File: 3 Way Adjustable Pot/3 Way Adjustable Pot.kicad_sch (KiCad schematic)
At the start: 26 parts, among them SW1 SW_MEC_5E, SW2 SW_MEC_5E, SW3 SW_MEC_5E, SW4 SW_MEC_5E, U1 74HC14, U2 74LS28, U3 74HC74, U4 74HC14, U6 74LS157, U7 LM555xN

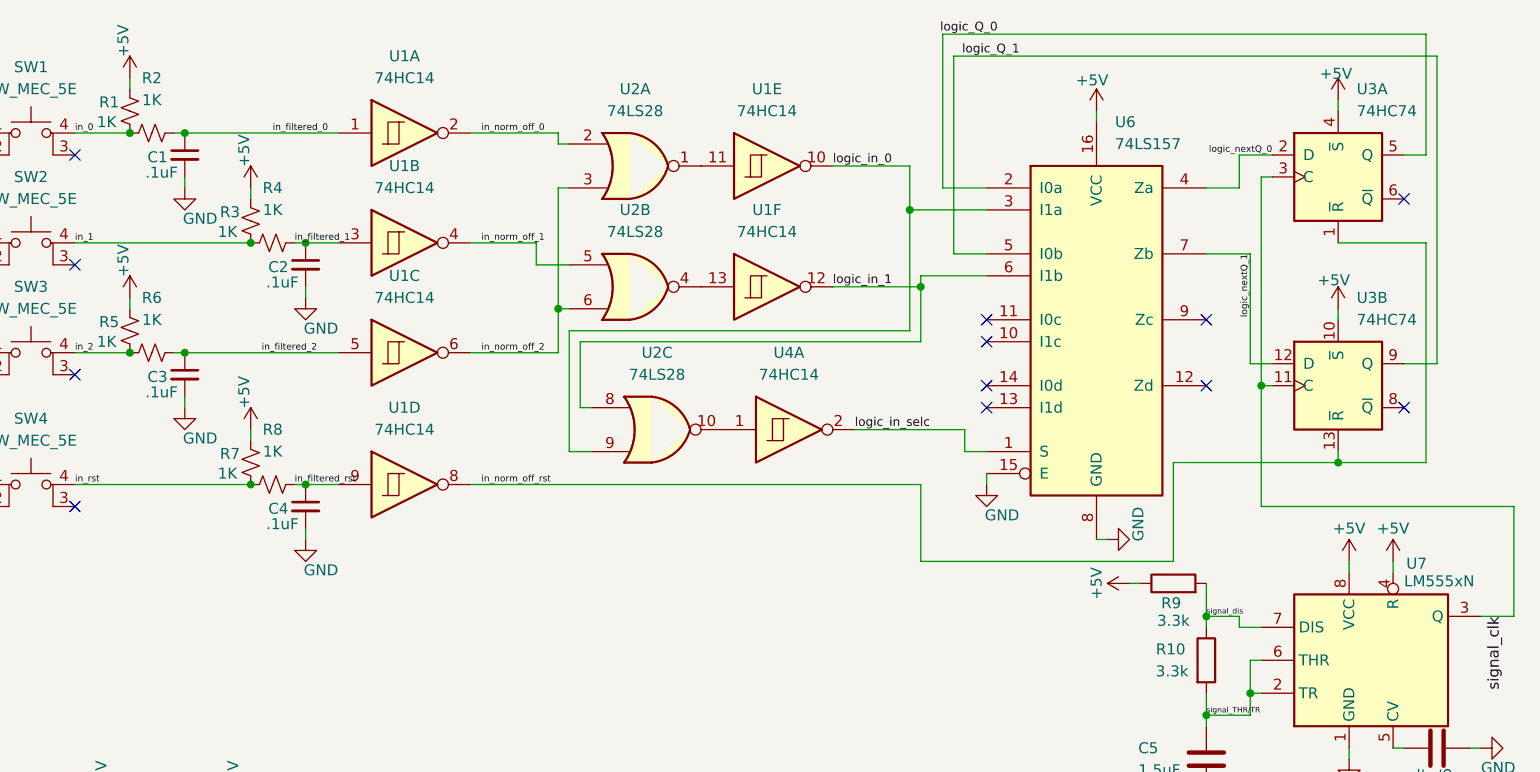
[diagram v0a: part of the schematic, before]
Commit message: add commits to 3 way adjustable pot
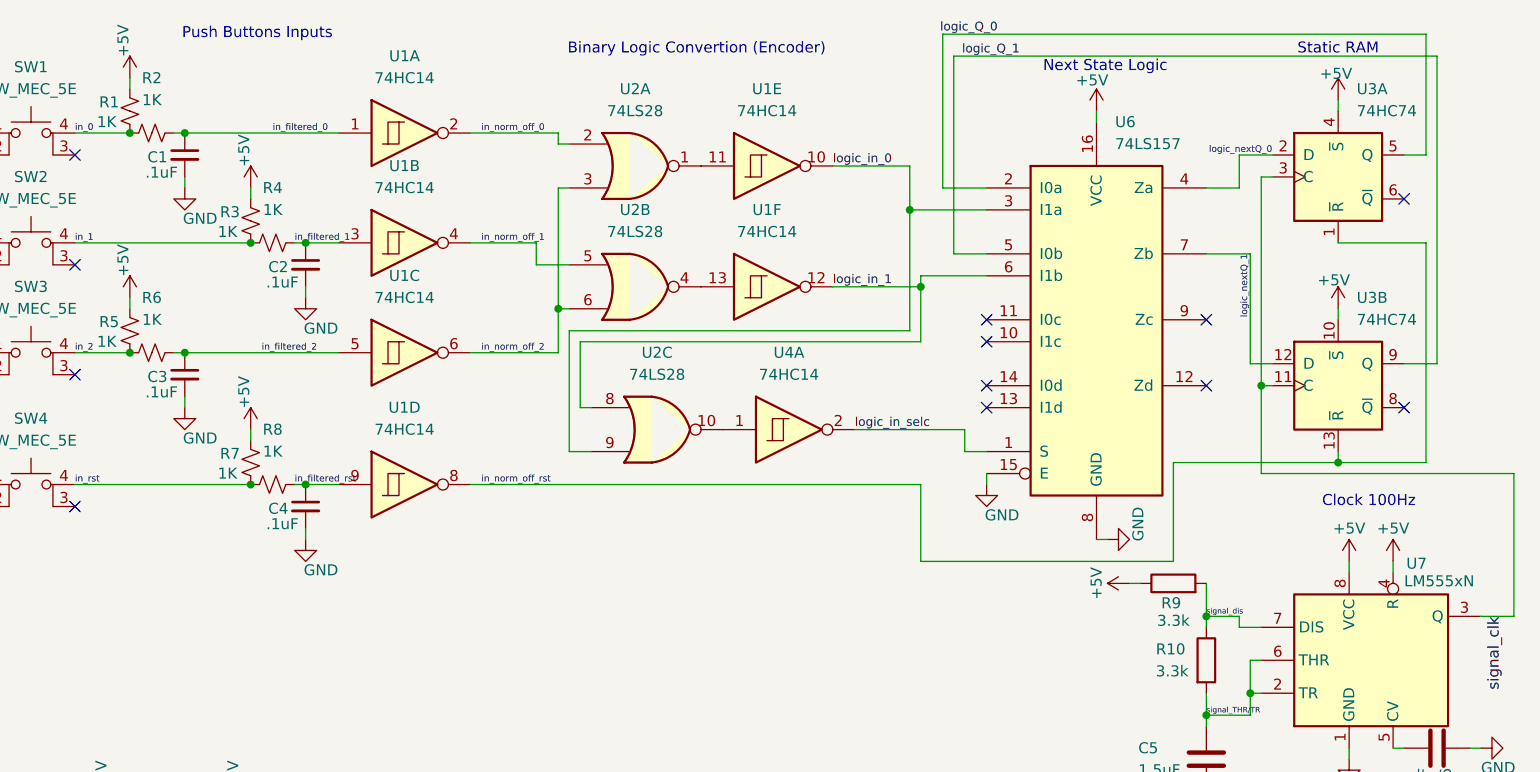
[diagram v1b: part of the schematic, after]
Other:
- note added: "Binary Logic Convertion (Encoder)"
- note added: "Clock 100Hz"
- note added: "Next State Logic"
- note added: "Push Buttons Inputs"
- note added: "Static RAM"
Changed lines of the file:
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@@
 		(rev "1")
 	)
+	(text "Push Buttons Inputs\n "
+		(exclude_from_sim no)
+		(at 51.562 14.986 0)
+		(effects
+			(font
+				(size 1.27 1.27)
+			)
+		)
+	)
+	(text "Clock 100Hz"
+		(exclude_from_sim no)
+		(at 180.086 68.072 0)
+		(effects
+			(font
+				(size 1.27 1.27)
+			)
+		)
+	)
+	(text "Binary Logic Convertion (Encoder)\n"
+		(exclude_from_sim no)
+		(at 102.362 15.748 0)
+		(effects
+			(font
+				(size 1.27 1.27)
+			)
+		)
+	)
+	(text "Static RAM"
+		(exclude_from_sim no)
+		(at 176.53 15.748 0)
+		(effects
+			(font
+				(size 1.27 1.27)
+			)
+		)
+	)
+	(text "Next State Logic \n"
+		(exclude_from_sim no)
+		(at 149.606 17.78 0)
+		(effects
+			(font
+				(size 1.27 1.27)
+			)
+		)
+	)
 	(junction
 		(at 36.83 25.4)
@@
 	(wire
 		(pts
-			(xy 196.85 81.28) (xy 196.85 68.58)
+			(xy 196.85 81.28) (xy 196.85 64.77)
 		)
 		(stroke
@@
 	(wire
 		(pts
-			(xy 167.64 54.61) (xy 167.64 68.58)
+			(xy 167.64 54.61) (xy 167.64 64.77)
 		)
 		(stroke
@@
 	(wire
 		(pts
-			(xy 196.85 68.58) (xy 167.64 68.58)
-		)
-		(stroke
+			(xy 196.85 64.77) (xy 167.64 64.77)
+		)
+		(stroke

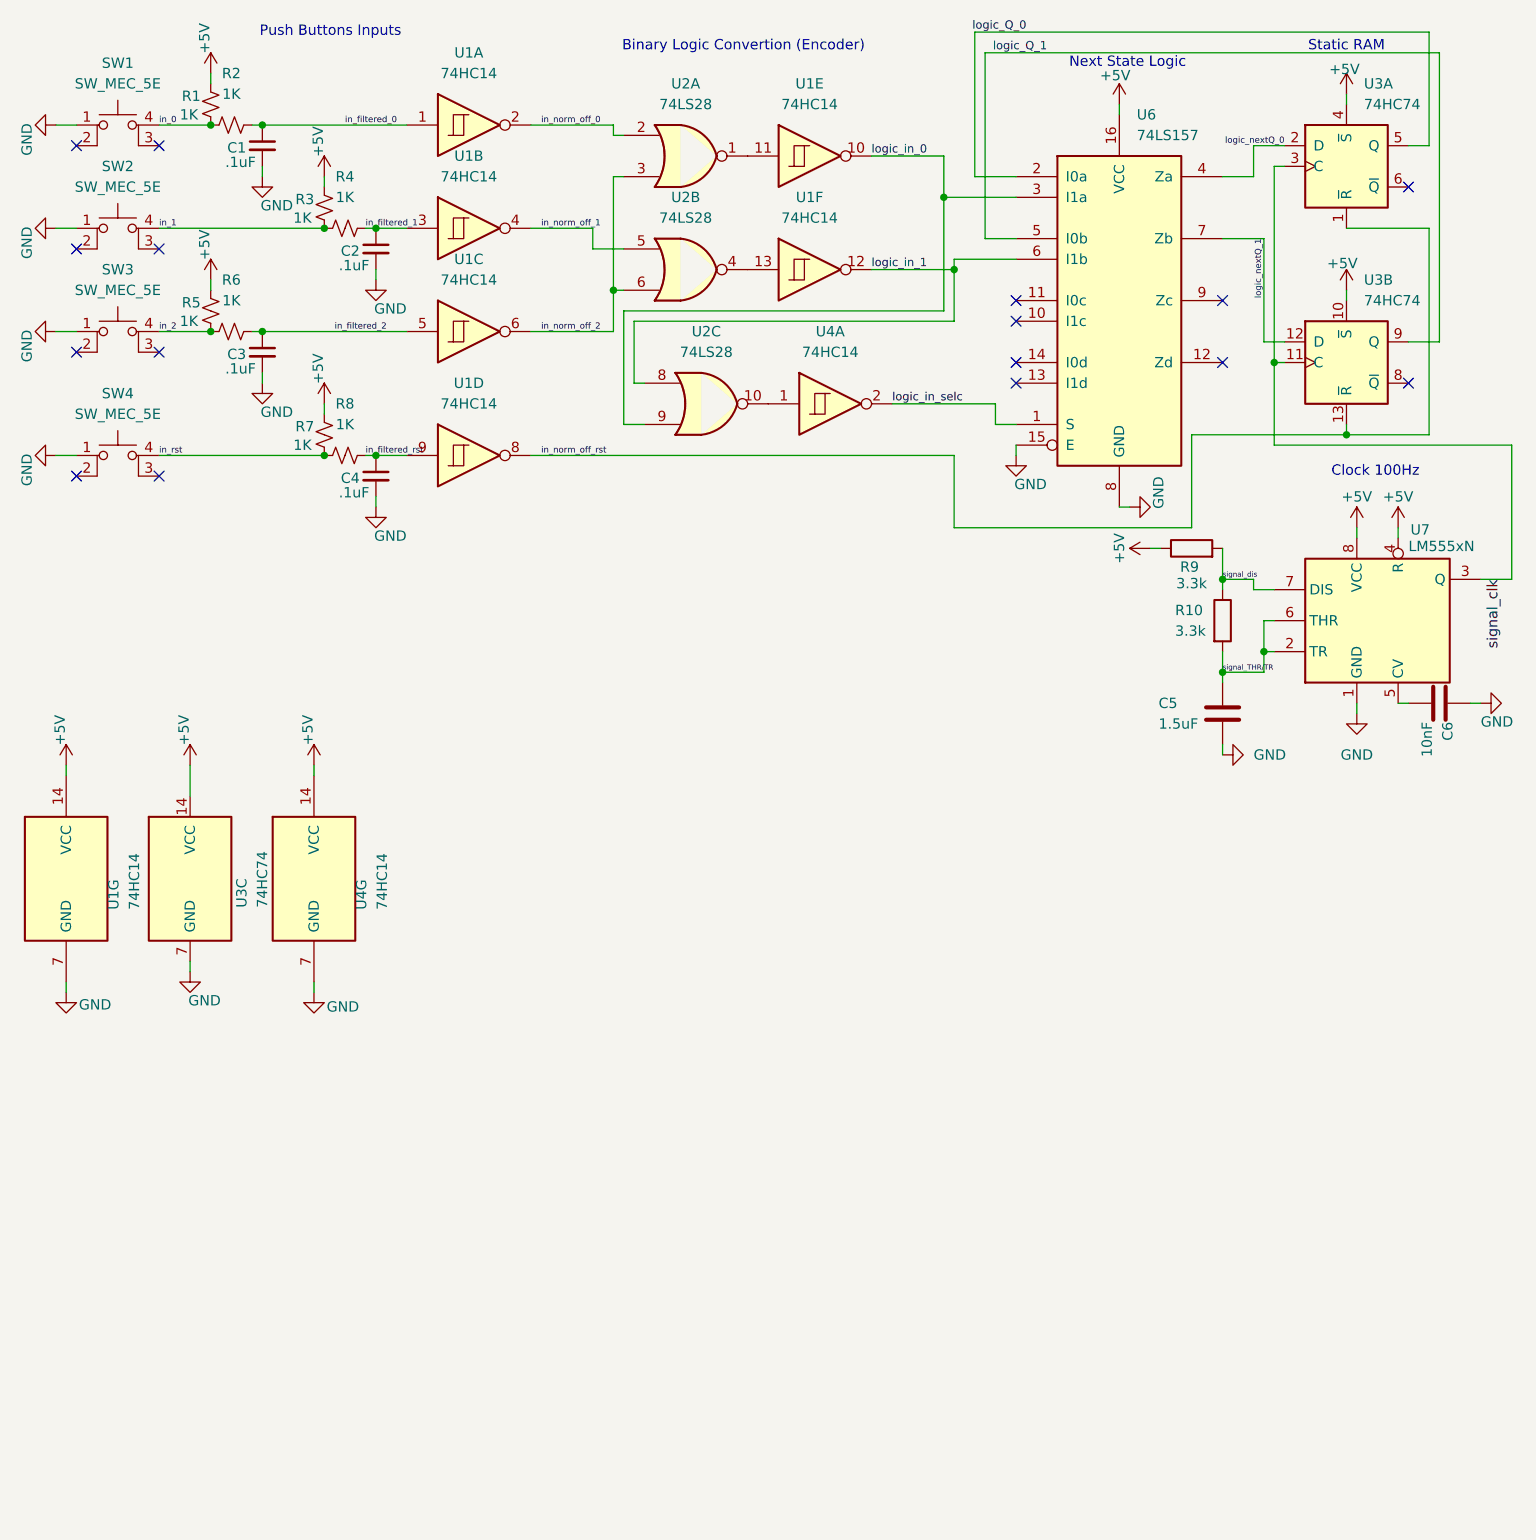
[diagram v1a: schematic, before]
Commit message: Design Phase Complete for Adjestable Pot
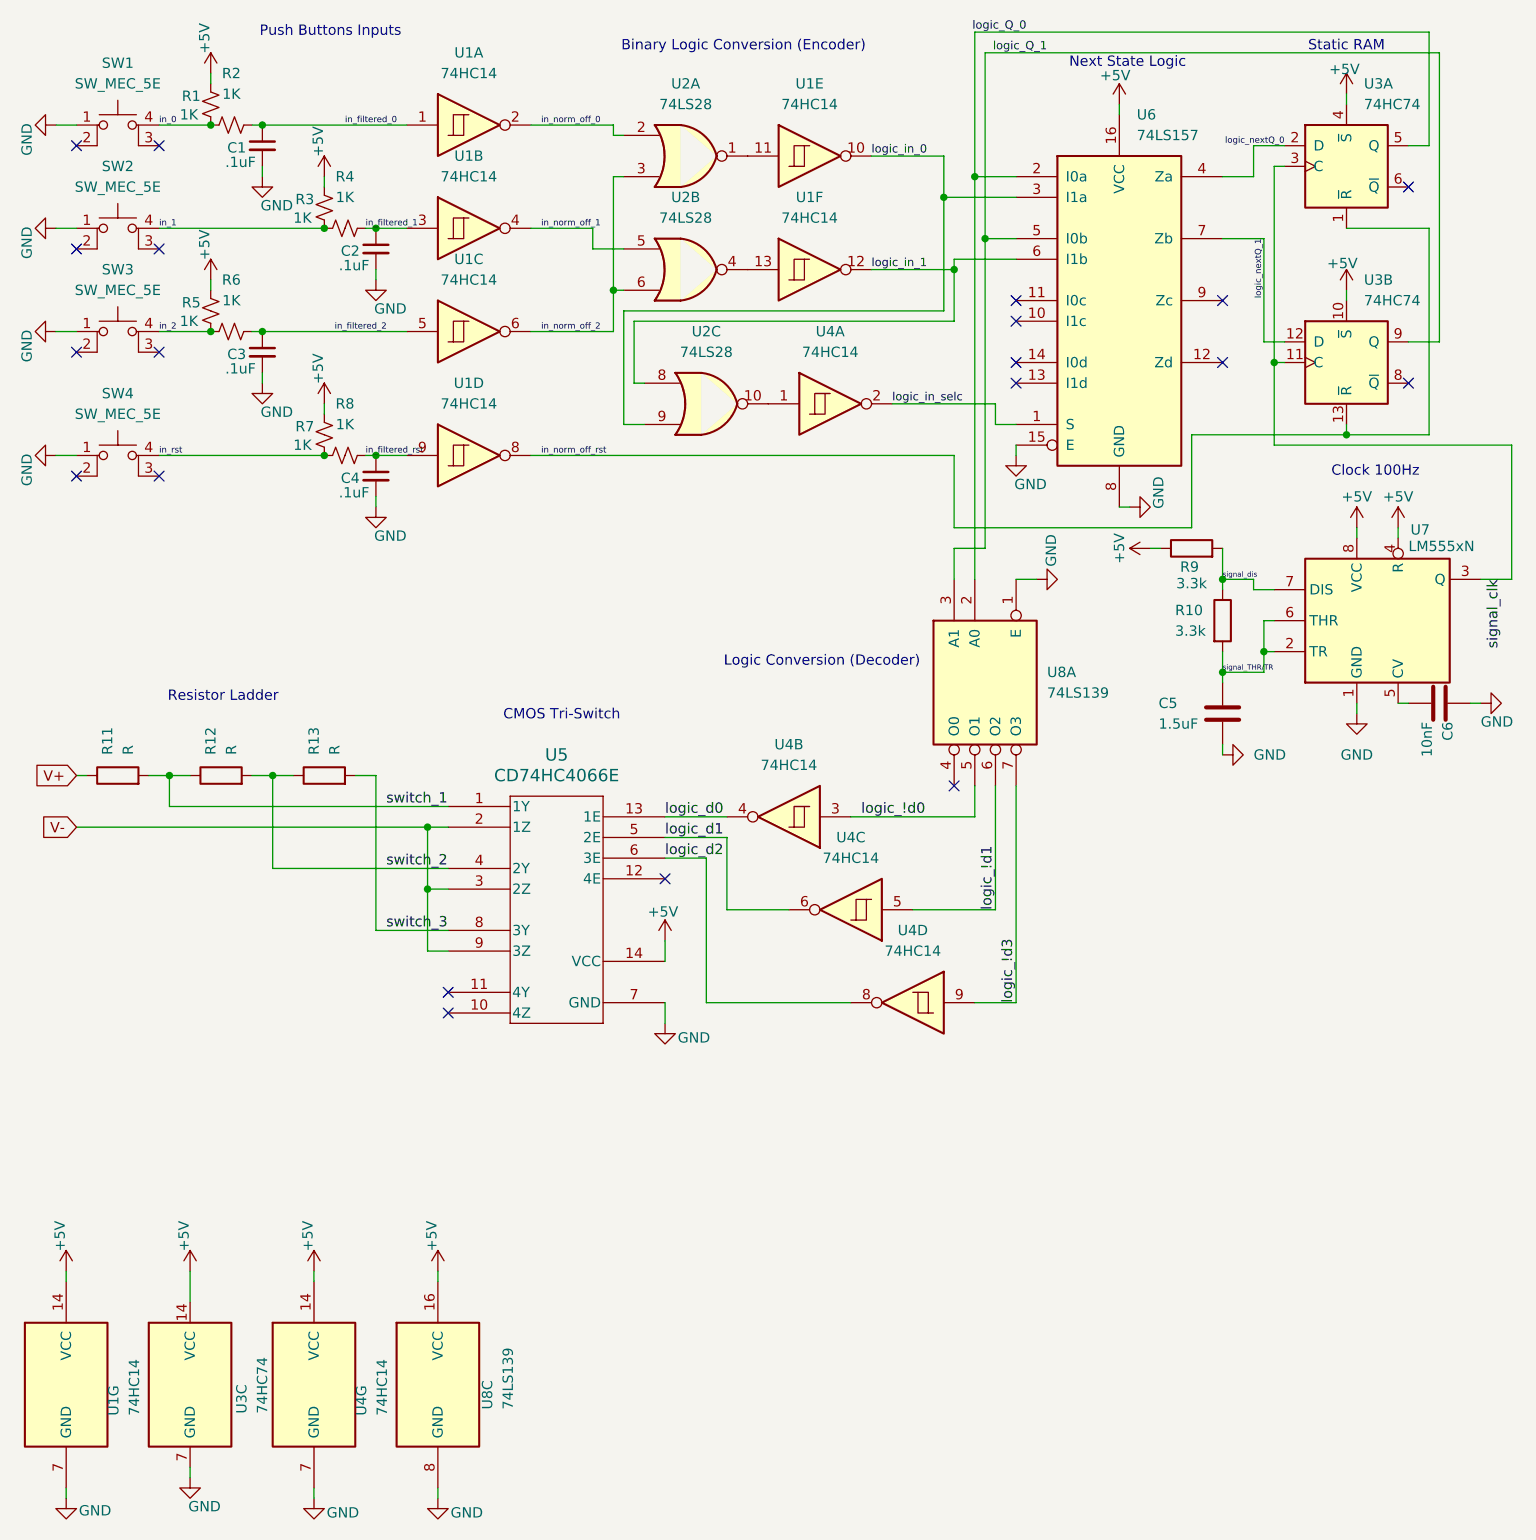
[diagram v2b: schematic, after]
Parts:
- added R11, R12, R13: R, symbol Device:R
- added unit 4 of U4
- added unit 2 of U4
- added unit 3 of U4
- added U5: CD74HC4066E, N14, symbol 74HC4006:CD74HC4066E
- added U8: 74LS139, symbol 74xx:74LS139
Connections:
- net +5V: now also U5.14 (VCC), U8.16 (VCC)
- net GND: now also U5.7 (GND), U8.1 (E), U8.8 (GND)
- net logic_Q_0: now also U8.2 (A0)
- net logic_Q_1: now also U8.3 (A1)
- new net V+: R11.1
- new net V-: U5.2 (1Z), U5.3 (2Z), U5.9 (3Z)
- new net logic_!d0: U4.3, U8.5 (O1)
- new net logic_!d1: U4.5, U8.6 (O2)
- new net logic_!d3: U4.9, U8.7 (O3)
- new net logic_d0: U4.4, U5.13 (1E)
- new net logic_d1: U4.6, U5.5 (2E)
- new net logic_d2: U4.8, U5.6 (3E)
- new net switch_1: R11.2, R12.1, U5.1 (1Y)
- new net switch_2: R12.2, R13.1, U5.4 (2Y)
- new net switch_3: R13.2, U5.8 (3Y)
- no-connect marks 16 -> 20
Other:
- note added: "Binary Logic Conversion (Encoder)"
- note added: "CMOS Tri-Switch"
- note added: "Logic Conversion (Decoder)"
- note added: "Resistor Ladder"
- note removed: "Binary Logic Convertion (Encoder)"
- moved on the sheet: U1G, U3C, U4G
